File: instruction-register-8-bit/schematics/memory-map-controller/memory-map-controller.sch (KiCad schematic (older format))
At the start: 6 parts, among them U1 74LS21, U2 74LS04, U3 74LS08, U4 74HCT238, U5 74HCT238, U6 74LS32

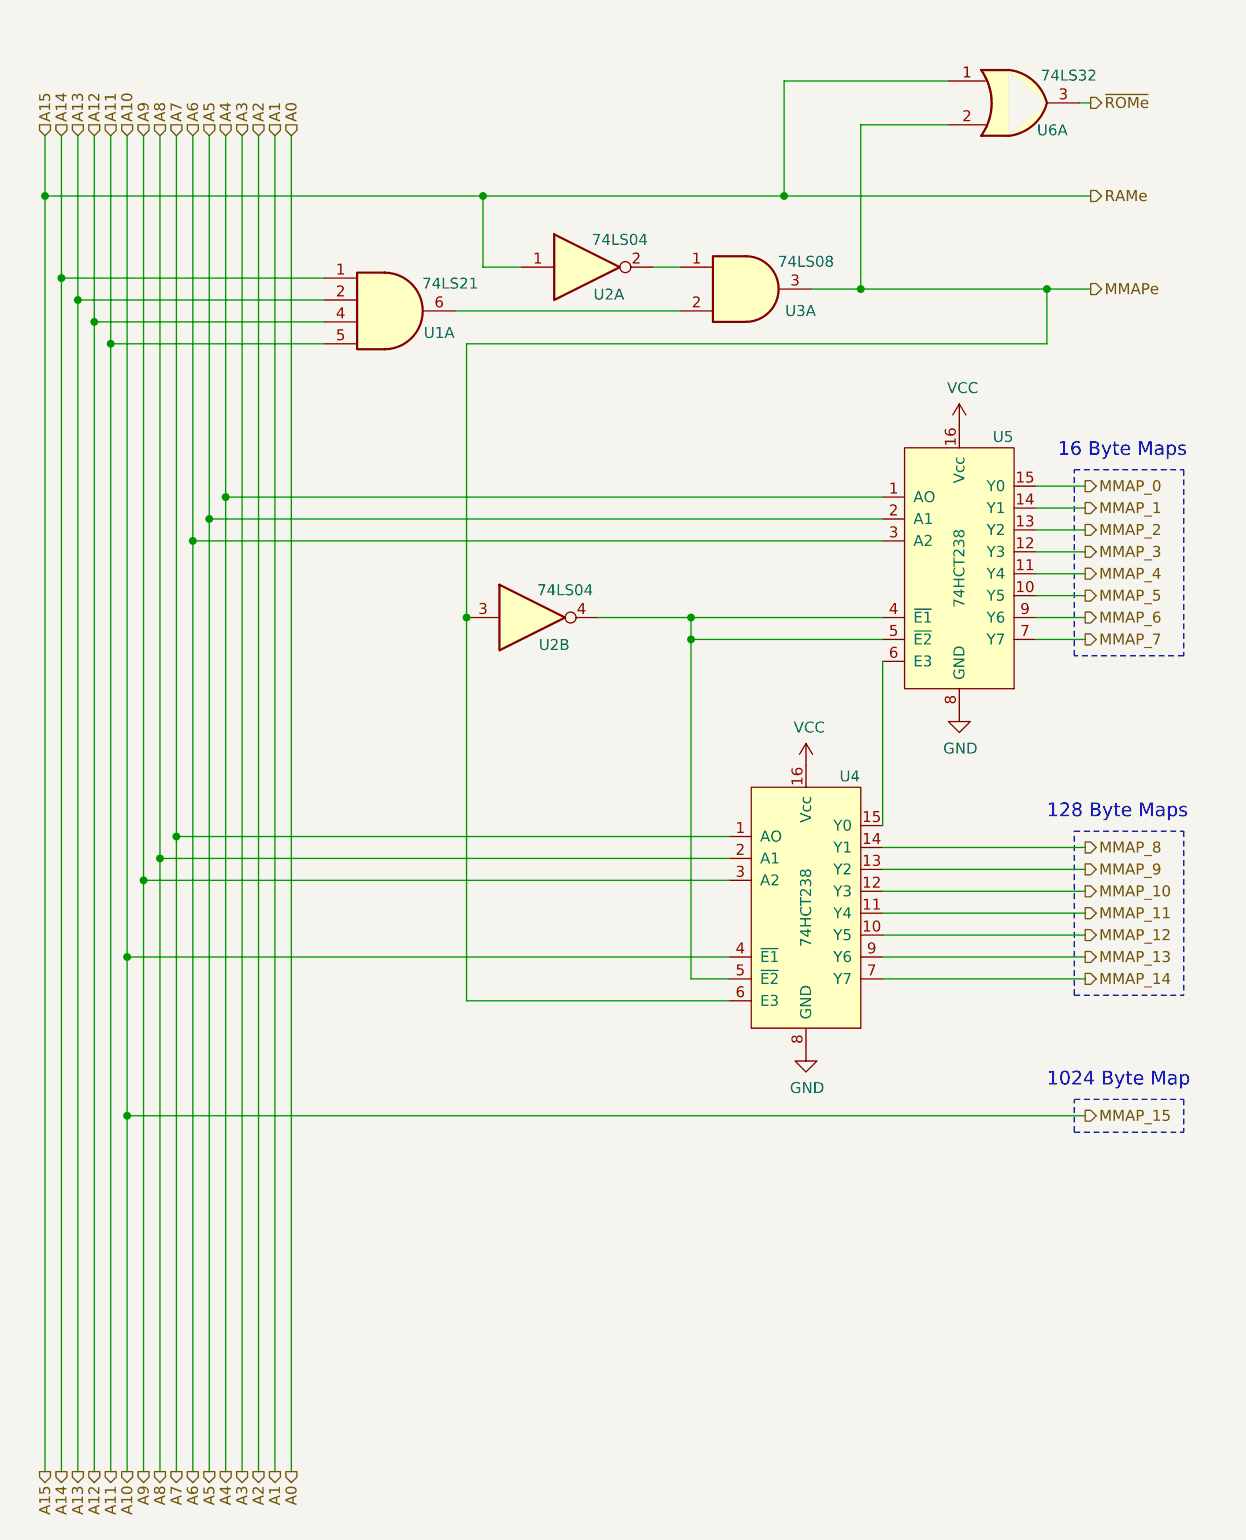
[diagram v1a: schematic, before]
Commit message: seperated RAM and ROM modules
In order to simplify each, the RAM and ROM modules are seperated and no longer share a common connection to the data bus. Also added support for addres line A16, though it is tied to ground and outherwise unused in this design
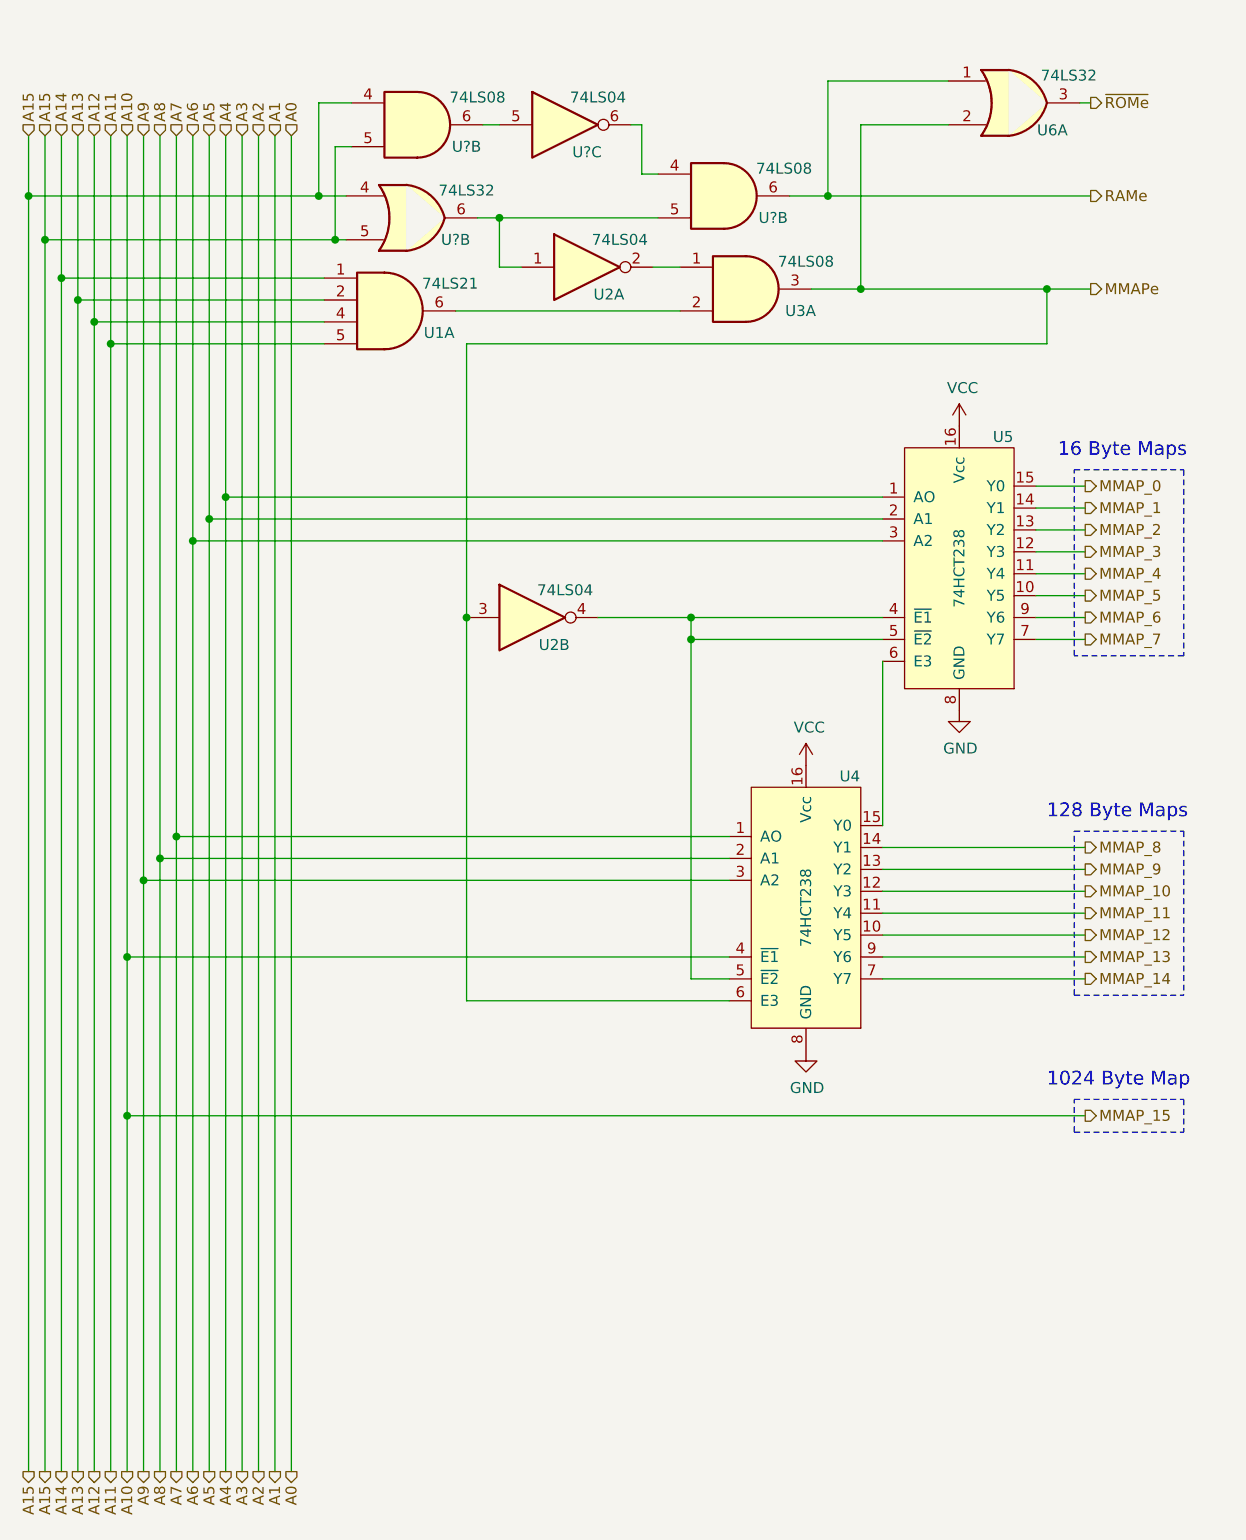
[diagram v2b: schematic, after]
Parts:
- added U?: 74LS32, symbol 74xx:74LS32
- added U? (x2): 74LS08, symbol 74xx:74LS08
- added U?: 74LS04, symbol 74xx:74LS04
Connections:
- net A15: now also U?.4, U?.4, U?.5, U?.5; no longer U2.1, U6.1
- new net: U2.1, U?.5, U?.6
- new net: U?.5, U?.6
- new net: U?.4, U?.6
- new net RAMe: U6.1, U?.6
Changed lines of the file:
@@
 Wire Wire Line
 	6225 4900 5300 4900
-Wire Wire Line
-	1475 1050 1475 1325
-Connection ~ 1475 1325
-Wire Wire Line
-	1475 1325 1475 7150
 $Comp
 L 74xx:74LS08 U3
@@
 1024 Byte Map
 Wire Wire Line
-	1475 1325 3475 1325
-Wire Wire Line
-	3650 1650 3475 1650
-Wire Wire Line
-	3475 1650 3475 1325
-Connection ~ 3475 1325
-Wire Wire Line
-	3475 1325 4850 1325
+	3650 1650 3550 1650
 $Comp
 L 74xx:74LS32 U6
@@
 $EndComp
 Wire Wire Line
-	4850 1325 4850 800
-Wire Wire Line
-	4850 800  5600 800
-Connection ~ 4850 1325
-Wire Wire Line
-	4850 1325 6250 1325
-Wire Wire Line
 	5200 1750 5200 1000
 Wire Wire Line
@@
 Wire Notes Line
 	6175 5600 6675 5600
+Text HLabel 1400 1050 1    50   Input ~ 0
+A15
+Text HLabel 1400 7150 3    50   Output ~ 0
+A15
+Wire Wire Line
+	1400 1050 1400 1325
+Wire Wire Line
+	1475 1050 1475 1525
+$Comp
+L 74xx:74LS32 U?
+U 2 1 60FC6A93
+P 3150 1425
+F 0 "U?" H 3350 1325 50  0000 C CNN
+F 1 "74LS32" H 3400 1550 50  0000 C CNN
+F 2 "" H 3150 1425 50  0001 C CNN
+F 3 "http://www.ti.com/lit/gpn/sn74LS32" H 3150 1425 50  0001 C CNN
+	2    3150 1425
+	1    0    0    -1
+$EndComp
+Wire Wire Line
+	2850 1525 2800 1525
+Connection ~ 1475 1525
+Wire Wire Line
+	1475 1525 1475 7150
+Wire Wire Line
+	2850 1325 2725 1325
+Connection ~ 1400 1325
+Wire Wire Line
+	1400 1325 1400 7150
+$Comp
+L 74xx:74LS08 U?
+U 2 1 60FD347A
+P 3175 1000
+F 0 "U?" H 3400 900 50  0000 C CNN
+F 1 "74LS08" H 3450 1125 50  0000 C CNN
+F 2 "" H 3175 1000 50  0001 C CNN
+F 3 "http://www.ti.com/lit/gpn/sn74LS08" H 3175 1000 50  0001 C CNN
+	2    3175 1000
+	1    0    0    -1
+$EndComp
+Wire Wire Line
+	2875 1100 2800 1100
+Wire Wire Line
+	2800 1100 2800 1525
+Connection ~ 2800 1525
+Wire Wire Line
+	2800 1525 1475 1525
+Wire Wire Line
+	2875 900  2725 900
+Wire Wire Line
+	2725 900  2725 1325
+Connection ~ 2725 1325
+Wire Wire Line
+	2725 1325 1400 1325
+$Comp
+L 74xx:74LS04 U?
+U 3 1 60FDE6A9
+P 3850 1000
+F 0 "U?" H 3950 875 50  0000 C CNN
+F 1 "74LS04" H 4000 1125 50  0000 C CNN
+F 2 "" H 3850 1000 50  0001 C CNN
+F 3 "http://www.ti.com/lit/gpn/sn74LS04" H 3850 1000 50  0001 C CNN
+	3    3850 1000
+	1    0    0    -1
+$EndComp
+$Comp
+L 74xx:74LS08 U?
+U 2 1 60FE27D8
+P 4575 1325
+F 0 "U?" H 4800 1225 50  0000 C CNN
+F 1 "74LS08" H 4850 1450 50  0000 C CNN
+F 2 "" H 4575 1325 50  0001 C CNN
+F 3 "http://www.ti.com/lit/gpn/sn74LS08" H 4575 1325 50  0001 C CNN
+	2    4575 1325
+	1    0    0    -1
+$EndComp
+Wire Wire Line
+	3450 1425 3550 1425
+Wire Wire Line
+	3550 1650 3550 1425
+Connection ~ 3550 1425
+Wire Wire Line
+	3550 1425 4275 1425
+Wire Wire Line
+	3475 1000 3550 1000
+Wire Wire Line
+	4150 1000 4200 1000
+Wire Wire Line
+	4200 1000 4200 1225
+Wire Wire Line
+	4200 1225 4275 1225
+Wire Wire Line
+	4875 1325 5050 1325
+Wire Wire Line
+	5050 1325 5050 800
+Wire Wire Line
+	5050 800  5600 800
+Connection ~ 5050 1325
+Wire Wire Line
+	5050 1325 6250 1325
 $EndSCHEMATC

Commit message: updated annotations
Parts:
- gave numbers to parts that had none: 3
- renumbered U6 to U4
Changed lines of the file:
@@
 	3650 1650 3550 1650
 $Comp
-L 74xx:74LS32 U6
+L 74xx:74LS32 U4
 U 1 1 60ED1285
 P 5900 900
-F 0 "U6" H 6075 775 50  0000 C CNN
+F 0 "U4" H 6075 775 50  0000 C CNN
 F 1 "74LS32" H 6150 1025 50  0000 C CNN
 F 2 "" H 5900 900 50  0001 C CNN
@@
 	6175 5600 6675 5600
 Text HLabel 1400 1050 1    50   Input ~ 0
-A15
+A16
 Text HLabel 1400 7150 3    50   Output ~ 0
 A15
@@
 	1475 1050 1475 1525
 $Comp
-L 74xx:74LS32 U?
+L 74xx:74LS32 U4
 U 2 1 60FC6A93
 P 3150 1425
-F 0 "U?" H 3350 1325 50  0000 C CNN
+F 0 "U4" H 3350 1325 50  0000 C CNN
 F 1 "74LS32" H 3400 1550 50  0000 C CNN
 F 2 "" H 3150 1425 50  0001 C CNN
@@
 	1400 1325 1400 7150
 $Comp
-L 74xx:74LS08 U?
+L 74xx:74LS08 U3
 U 2 1 60FD347A
 P 3175 1000
-F 0 "U?" H 3400 900 50  0000 C CNN
+F 0 "U3" H 3400 900 50  0000 C CNN
 F 1 "74LS08" H 3450 1125 50  0000 C CNN
 F 2 "" H 3175 1000 50  0001 C CNN
@@
 	2725 1325 1400 1325
 $Comp
-L 74xx:74LS04 U?
+L 74xx:74LS04 U2
 U 3 1 60FDE6A9
 P 3850 1000
-F 0 "U?" H 3950 875 50  0000 C CNN
+F 0 "U2" H 3950 875 50  0000 C CNN
 F 1 "74LS04" H 4000 1125 50  0000 C CNN
 F 2 "" H 3850 1000 50  0001 C CNN
@@
 $EndComp
 $Comp
-L 74xx:74LS08 U?
+L 74xx:74LS08 U3
 U 2 1 60FE27D8
 P 4575 1325
-F 0 "U?" H 4800 1225 50  0000 C CNN
+F 0 "U3" H 4800 1225 50  0000 C CNN
 F 1 "74LS08" H 4850 1450 50  0000 C CNN
 F 2 "" H 4575 1325 50  0001 C CNN

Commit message: adjustments based on construction layout
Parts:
- U4: value 74HCT238 -> 74LS32
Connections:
- net A15: now also U3.10, U3.9, U4.10, U4.9; no longer U3.4, U3.5, U4.4, U4.5
- net MMAPe: now also U3.6, U4.13; no longer U3.3, U4.2
- net RAMe: now also U3.11, U4.12; no longer U3.6, U4.1
- net ~ROMe: now also U4.11; no longer U4.3
- net at U1.6: now also U3.5; no longer U3.2
- new net: U2.5, U3.12, U4.8
- new net: U2.9, U3.8
- new net: U2.8, U3.13
- new net: U2.6, U3.4
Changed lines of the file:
@@
 $Comp
 L 74xx:74LS04 U2
-U 1 1 610A4EC8
+U 3 1 610A4EC8
 P 3950 1650
 F 0 "U2" H 4050 1525 50  0000 C CNN
@@
 F 2 "" H 3950 1650 50  0001 C CNN
 F 3 "http://www.ti.com/lit/gpn/sn74LS04" H 3950 1650 50  0001 C CNN
-	1    3950 1650
+	3    3950 1650
 	1    0    0    -1
 $EndComp
@@
 P 4950 4550
 F 0 "U4" H 5150 5125 50  0000 C CNN
-F 1 "74HCT238" V 4950 4525 50  0000 C CNN
+F 1 "74LS32" V 4950 4525 50  0000 C CNN
 F 2 "" H 4800 4375 50  0001 C CNN
-F 3 "" H 4800 4375 50  0001 C CNN
+F 3 "http://www.ti.com/lit/gpn/sn74LS32" H 4800 4375 50  0001 C CNN
 	1    4950 4550
 	1    0    0    -1
@@
 $Comp
 L 74xx:74LS08 U3
-U 1 1 6124CEFE
+U 2 1 6124CEFE
 P 4675 1750
 F 0 "U3" H 4925 1650 50  0000 C CNN
@@
 F 2 "" H 4675 1750 50  0001 C CNN
 F 3 "http://www.ti.com/lit/gpn/sn74LS08" H 4675 1750 50  0001 C CNN
-	1    4675 1750
+	2    4675 1750
 	1    0    0    -1
 $EndComp
@@
 $Comp
 L 74xx:74LS32 U4
-U 1 1 60ED1285
+U 4 1 60ED1285
 P 5900 900
 F 0 "U4" H 6075 775 50  0000 C CNN
@@
 F 2 "" H 5900 900 50  0001 C CNN
 F 3 "http://www.ti.com/lit/gpn/sn74LS32" H 5900 900 50  0001 C CNN
-	1    5900 900
+	4    5900 900
 	1    0    0    -1
 $EndComp
@@
 $Comp
 L 74xx:74LS32 U4
-U 2 1 60FC6A93
+U 3 1 60FC6A93
 P 3150 1425
 F 0 "U4" H 3350 1325 50  0000 C CNN
@@
 F 2 "" H 3150 1425 50  0001 C CNN
 F 3 "http://www.ti.com/lit/gpn/sn74LS32" H 3150 1425 50  0001 C CNN
-	2    3150 1425
+	3    3150 1425
 	1    0    0    -1
 $EndComp
@@
 $Comp
 L 74xx:74LS08 U3
-U 2 1 60FD347A
+U 3 1 60FD347A
 P 3175 1000
 F 0 "U3" H 3400 900 50  0000 C CNN
@@
 F 2 "" H 3175 1000 50  0001 C CNN
 F 3 "http://www.ti.com/lit/gpn/sn74LS08" H 3175 1000 50  0001 C CNN
-	2    3175 1000
+	3    3175 1000
 	1    0    0    -1
 $EndComp
@@
 $Comp
 L 74xx:74LS04 U2
-U 3 1 60FDE6A9
+U 4 1 60FDE6A9
 P 3850 1000
 F 0 "U2" H 3950 875 50  0000 C CNN
@@
 F 2 "" H 3850 1000 50  0001 C CNN
 F 3 "http://www.ti.com/lit/gpn/sn74LS04" H 3850 1000 50  0001 C CNN
-	3    3850 1000
+	4    3850 1000
 	1    0    0    -1
 $EndComp
 $Comp
 L 74xx:74LS08 U3
-U 2 1 60FE27D8
+U 4 1 60FE27D8
 P 4575 1325
 F 0 "U3" H 4800 1225 50  0000 C CNN
@@
 F 2 "" H 4575 1325 50  0001 C CNN
 F 3 "http://www.ti.com/lit/gpn/sn74LS08" H 4575 1325 50  0001 C CNN
-	2    4575 1325
-	1    0    0    -1
-$EndComp
-Wire Wire Line
+	4    4575 1325
+	1    0    0    1
+$EndComp
+Wire Wire Line

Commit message: tweaks and fixes
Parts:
- added unit 1 of U3
- renumbered U4 to U6
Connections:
- net A10: now also U3.2
- net MMAPe: now also U3.1
- new net MMAP_15: U3.3
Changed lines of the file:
@@
 $EndComp
 $Comp
-L common-symbols:74HCT238 U4
+L common-symbols:74HCT238 U6
 U 1 1 610C819E
 P 4950 4550
-F 0 "U4" H 5150 5125 50  0000 C CNN
+F 0 "U6" H 5150 5125 50  0000 C CNN
 F 1 "74LS32" V 4950 4525 50  0000 C CNN
 F 2 "" H 4800 4375 50  0001 C CNN
@@
 	4600 4800 1850 4800
 Connection ~ 1850 4800
-Wire Wire Line
-	1850 4800 1850 5525
 Wire Wire Line
 	4600 4450 1925 4450
@@
 Wire Wire Line
 	1850 1050 1850 4800
-Wire Wire Line
-	1850 5525 6225 5525
-Connection ~ 1850 5525
-Wire Wire Line
-	1850 5525 1850 7150
 Text HLabel 6225 5525 2    50   Output ~ 0
 MMAP_15
@@
 Wire Wire Line
 	5050 1325 6250 1325
+Wire Wire Line
+	4000 5525 6225 5525
+Wire Wire Line
+	1850 4800 1850 5625
+Wire Wire Line
+	3400 5625 1850 5625
+Connection ~ 1850 5625
+Wire Wire Line
+	1850 5625 1850 7150
+Wire Wire Line
+	3400 5000 3400 5425
+Connection ~ 3400 5000
+$Comp
+L 74xx:74LS08 U3
+U 1 1 611259B0
+P 3700 5525
+F 0 "U3" H 3700 5850 50  0000 C CNN
+F 1 "74LS08" H 3700 5759 50  0000 C CNN
+F 2 "" H 3700 5525 50  0001 C CNN
+F 3 "http://www.ti.com/lit/gpn/sn74LS08" H 3700 5525 50  0001 C CNN
+	1    3700 5525
+	1    0    0    -1
+$EndComp
 $EndSCHEMATC
